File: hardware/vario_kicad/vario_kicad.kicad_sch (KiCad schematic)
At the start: 0 parts

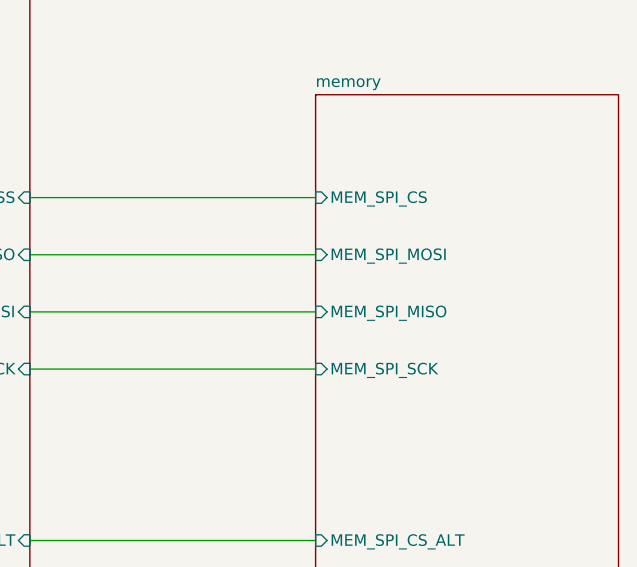
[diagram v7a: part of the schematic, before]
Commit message: fix memory schematic, update button switches
- fix miso/mosi mistake: miso->miso, mosi->mosi
- WKUP1 needs a rising edge to wake up the MCU, so all switch logic was
  reversed
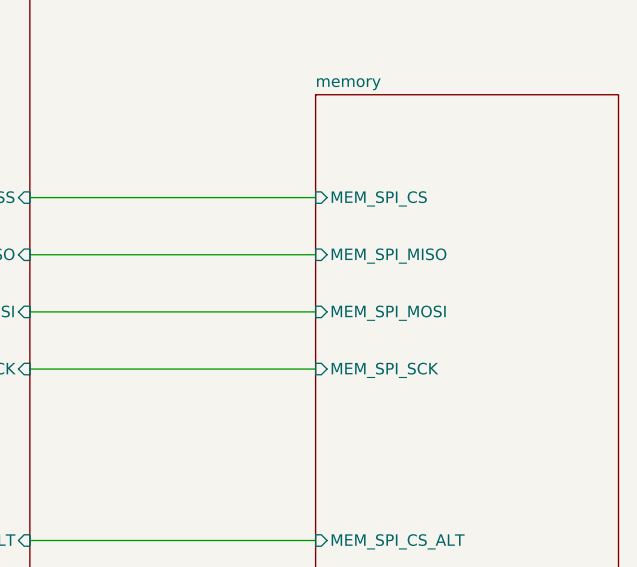
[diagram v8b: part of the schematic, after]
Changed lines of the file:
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@@
+	(wire
+		(pts
+			(xy 167.64 72.39) (xy 199.39 72.39)
+		)
+		(stroke
+			(width 0)
+			(type default)
+		)
+	)
 	(wire
 		(pts
@@
 	(wire
 		(pts
+			(xy 167.64 66.04) (xy 199.39 66.04)
+		)
+		(stroke
+			(width 0)
+			(type default)
+		)
+	)
+	(wire
+		(pts
 			(xy 105.41 138.43) (xy 133.35 138.43)
 		)
@@
 	(wire
 		(pts
-			(xy 167.64 72.39) (xy 199.39 72.39)
-		)
-		(stroke
-			(width 0)
-			(type default)
-		)
-	)
-	(wire
-		(pts
 			(xy 114.3 31.75) (xy 133.35 31.75)
 		)
@@
 		(pts
 			(xy 114.3 57.15) (xy 133.35 57.15)
-		)
-		(stroke
-			(width 0)
-			(type default)
-		)
-	)
-	(wire
-		(pts
-			(xy 167.64 66.04) (xy 199.39 66.04)
 		)
 		(stroke
@@
 		)
 		(pin "MEM_SPI_MISO" input
+			(at 199.39 66.04 180)
+			(effects
+				(font
+					(size 1.27 1.27)
+				)
+				(justify left)
+			)
+		)
+		(pin "MEM_SPI_MOSI" input
 			(at 199.39 72.39 180)
 			(effects
 				(font
-					(size 1.27 1.27)
-				)
-				(justify left)
-			)
-		)
-		(pin "MEM_SPI_MOSI" input
-			(at 199.39 66.04 180)
-			(effects
-				(font
